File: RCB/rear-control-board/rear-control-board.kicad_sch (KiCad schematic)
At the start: 19 parts, among them J1 Conn_01x23, J2 Conn_01x14, J3 Conn_01x08, K1 T9VV1K15-12S, U3 R-78B5.0-2.0

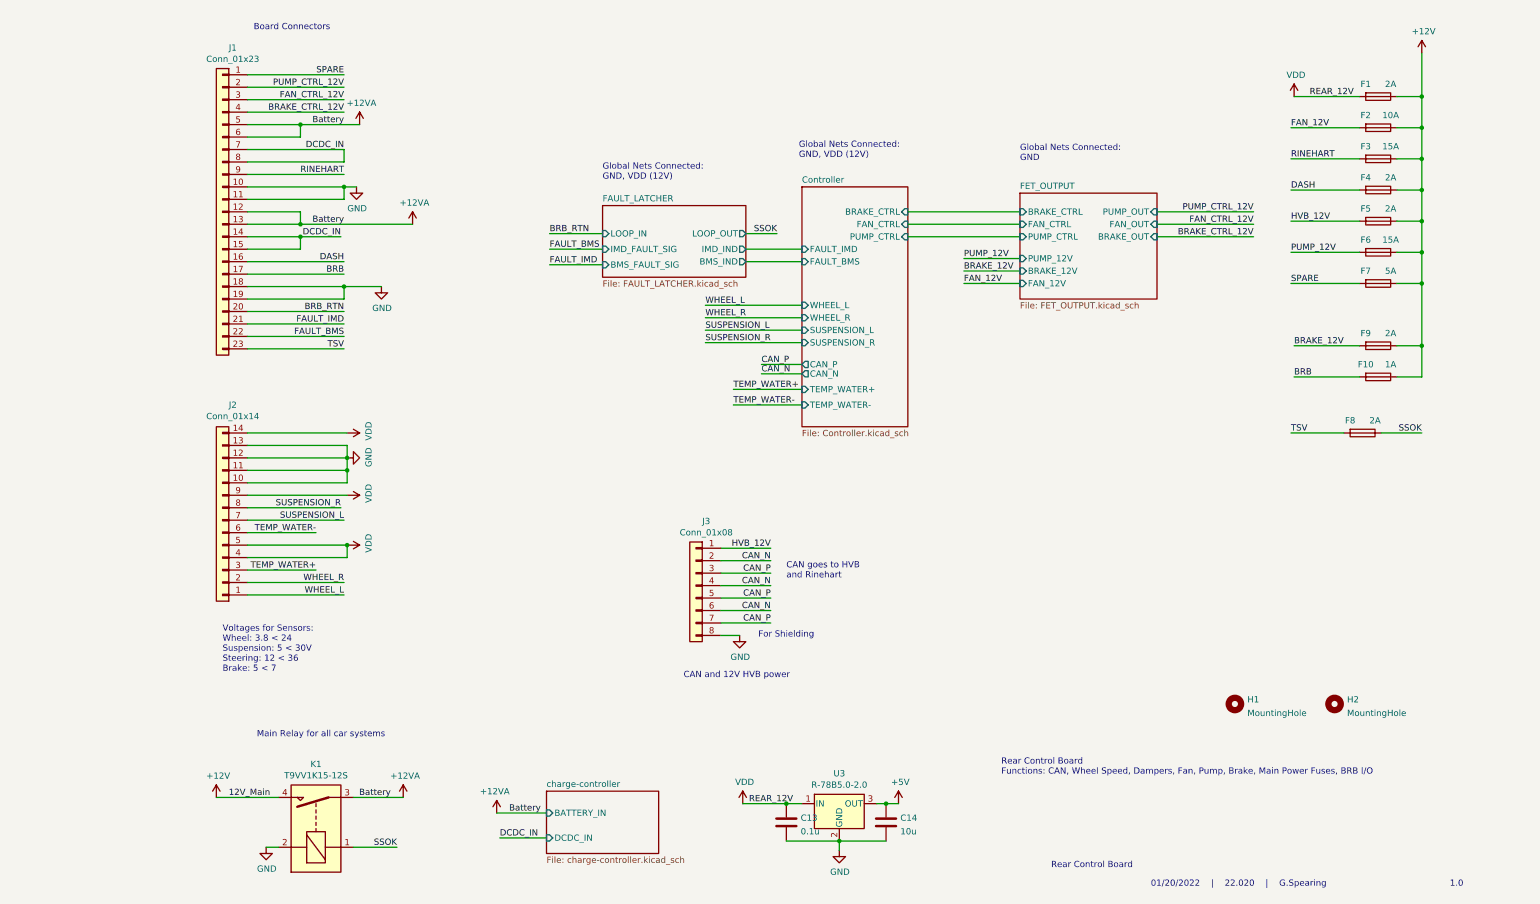
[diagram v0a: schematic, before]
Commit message: updating pinouts
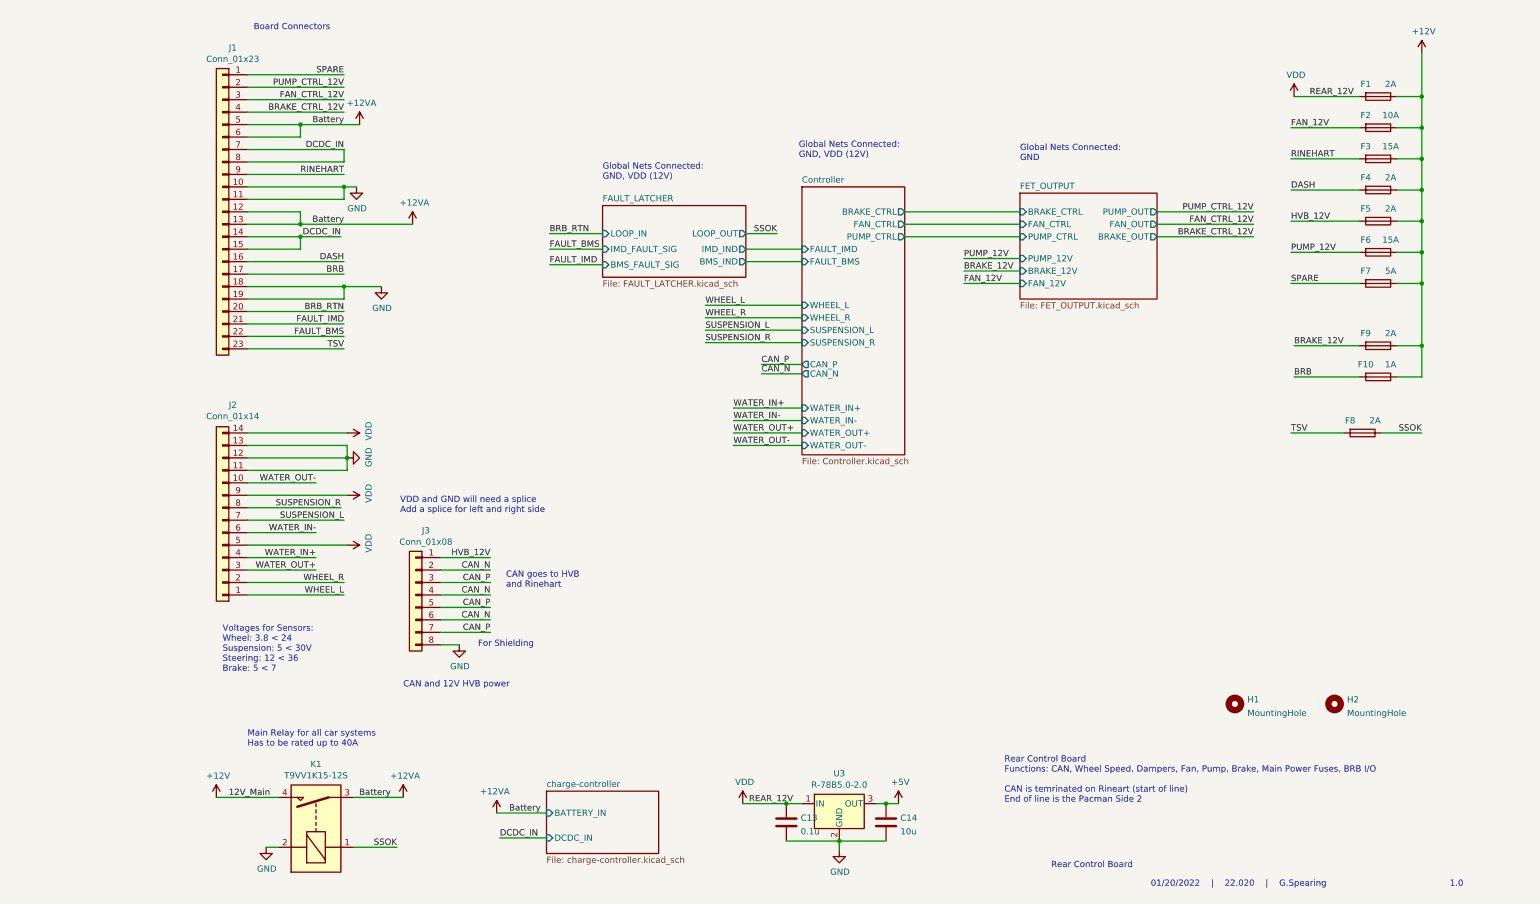
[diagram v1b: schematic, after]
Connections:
- net GND: no longer J2.10 (Pin_10)
- net VDD: no longer J2.4 (Pin_4)
- net TEMP_WATER+ renamed WATER_OUT+
- net TEMP_WATER- renamed WATER_IN-
- new net WATER_IN+: J2.4 (Pin_4)
- new net WATER_OUT-: J2.10 (Pin_10)
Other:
- sheet Controller ports: added WATER_IN+, WATER_IN-, WATER_OUT+, WATER_OUT-; removed TEMP_WATER+, TEMP_WATER-
- note added: "Main Relay for all car systems Has to be rated up to 40A"
- note added: "Rear Control Board Functions: CAN, Wheel Speed, Dampers, Fan, Pump, Brake, Main Power Fuses, BRB I/O CAN is temrinated on Rineart (start of line) End of line is the Pacman Side 2"
- note added: "VDD and GND will need a splice Add a splice for left and right side"
- note removed: "Main Relay for all car systems"
- note removed: "Rear Control Board Functions: CAN, Wheel Speed, Dampers, Fan, Pump, Brake, Main Power Fuses, BRB I/O"
- moved on the sheet: J3

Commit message: willem review notes
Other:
- note added: "DON'T FORGET INLINE FUSE FOR 12v"
- note added: "Power sensors off 5V line instead to reduce noise and help with power"
- note added: "RENAME ALL VDD TO INTERNAL 12V"
- note added: "Use VBus instead of VA"
- note added: "add sheet for fuses"
- note added: "checkout parts for temperature monitoring Look for NTC"
- note added: "protection -> TVS for the input"
- moved on the sheet: F1, F10, F2, F3, F4, F5, F6, F7, F8, F9, J1, K1

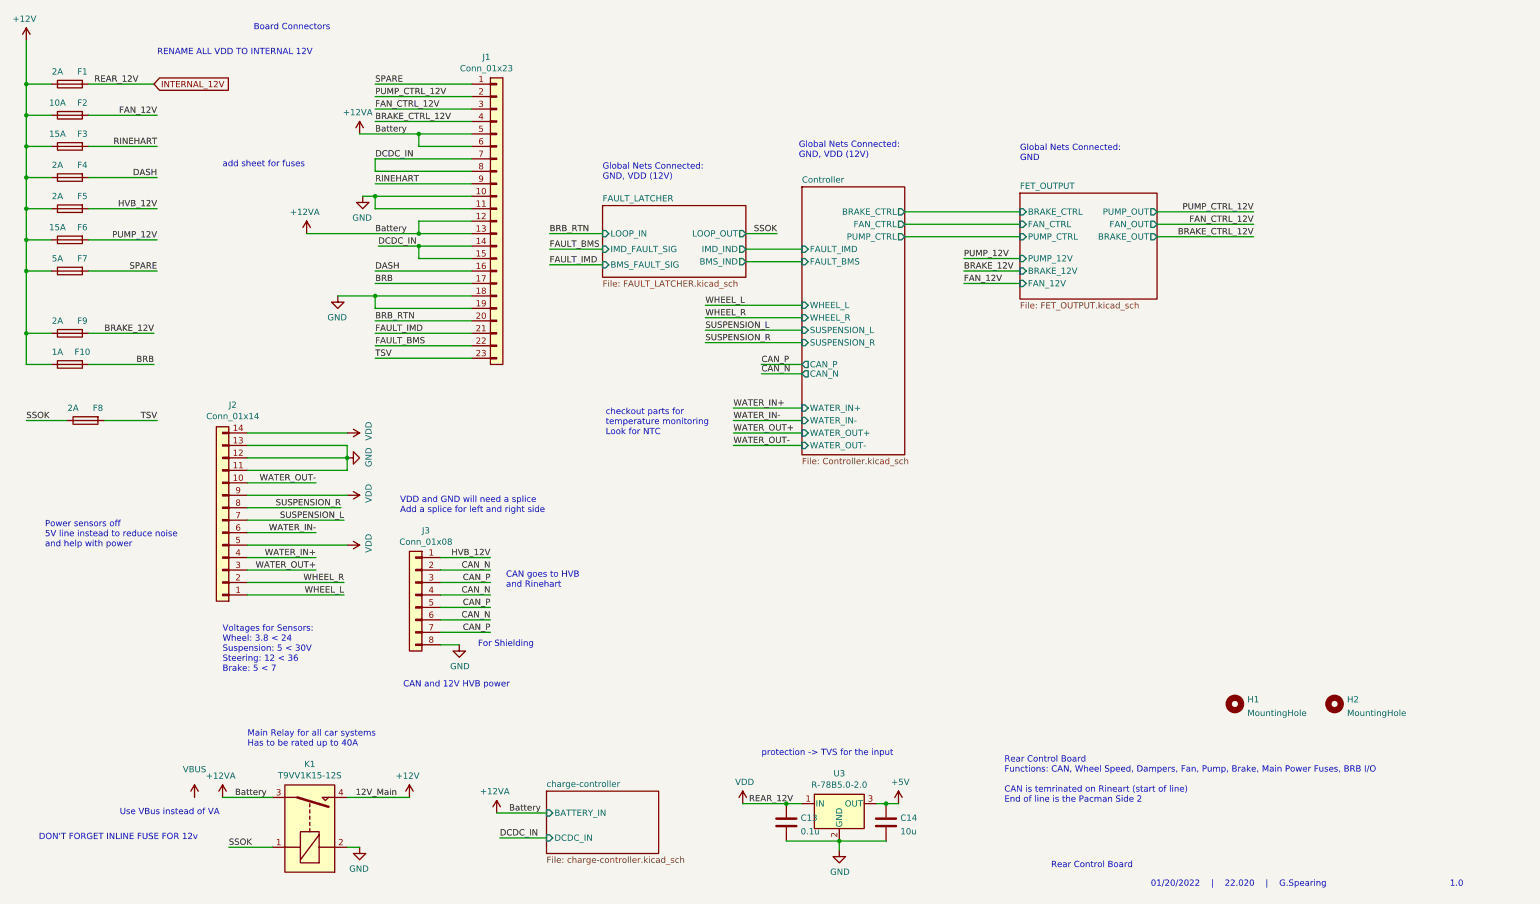
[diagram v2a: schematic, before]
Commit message: updating schem with design notes (major changes)
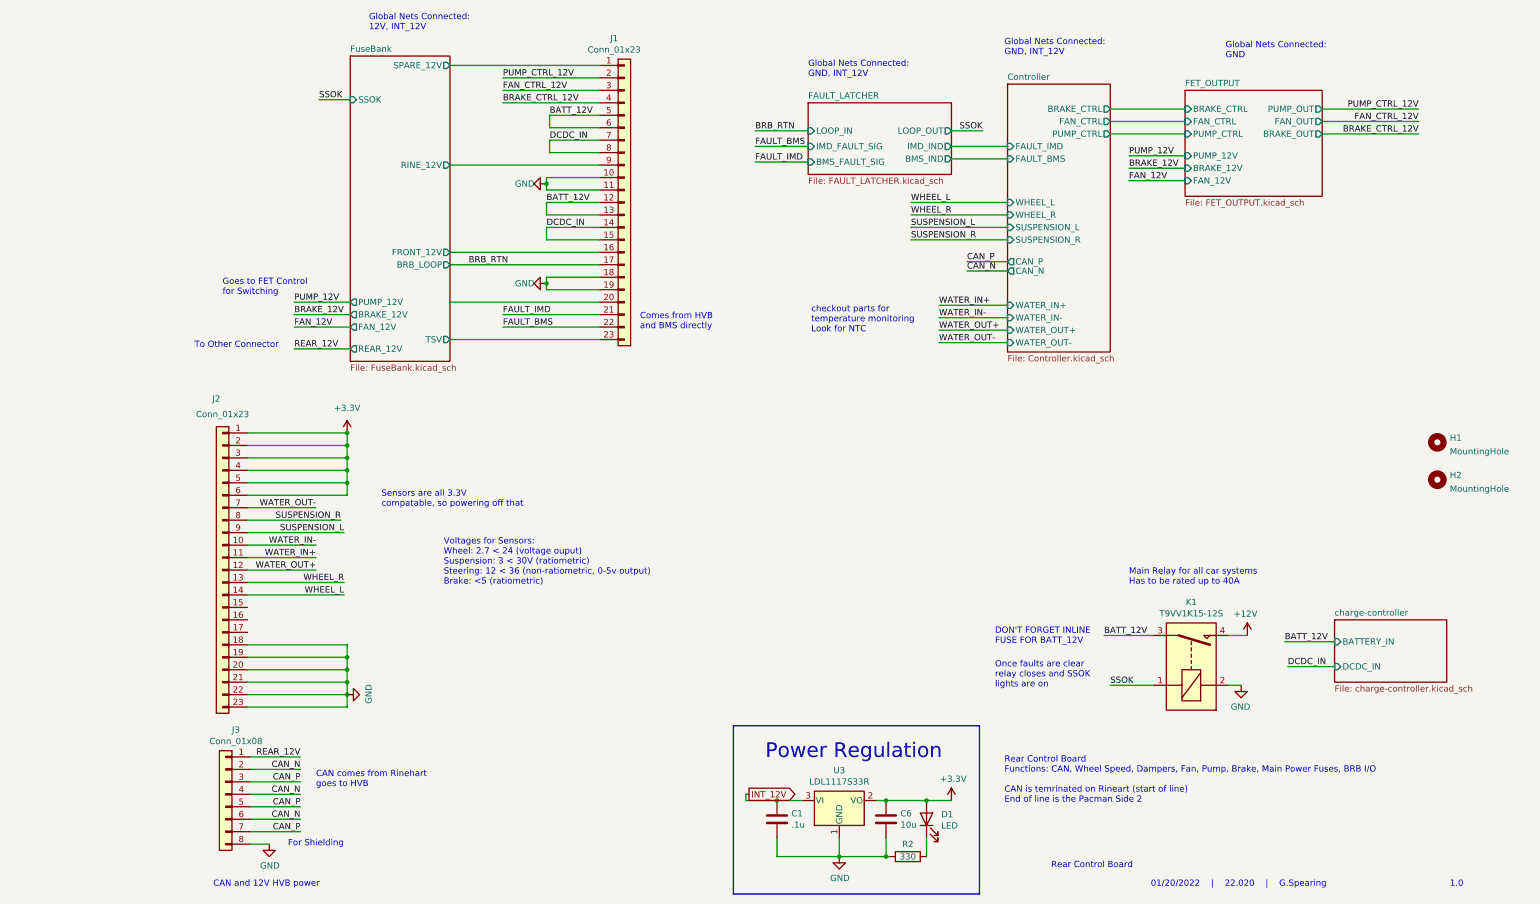
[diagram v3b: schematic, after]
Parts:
- removed C13: 0.1u, Capacitor_SMD:C_0603_1608Metric_Pad1.08x0.95mm_HandSolder, symbol Device:C
- removed C14: 10u, Capacitor_SMD:C_0603_1608Metric_Pad1.08x0.95mm_HandSolder, symbol Device:C
- removed F1, F4, F5, F8, F9: 2A, AERO_Footprints:Fuseholder_Blade_Mini_Keystone_3568, symbol Device:Fuse
- removed F10: 1A, AERO_Footprints:Fuseholder_Blade_Mini_Keystone_3568, symbol Device:Fuse
- removed F2: 10A, AERO_Footprints:Fuseholder_Blade_Mini_Keystone_3568, symbol Device:Fuse
- removed F3, F6: 15A, AERO_Footprints:Fuseholder_Blade_Mini_Keystone_3568, symbol Device:Fuse
- removed F7: 5A, AERO_Footprints:Fuseholder_Blade_Mini_Keystone_3568, symbol Device:Fuse
- removed J2: Conn_01x14, AERO_Footprints:TE_1-776266-1_14pin_Horizontal, symbol Connector_Generic:Conn_01x14
- removed U3: R-78B5.0-2.0, Converter_DCDC:Converter_DCDC_RECOM_R-78B-2.0_THT, symbol Regulator_Switching:R-78B5.0-2.0
- added C1: .1u, Capacitor_SMD:C_0603_1608Metric_Pad1.08x0.95mm_HandSolder, symbol Device:C
- added C6: 10u, Capacitor_SMD:C_0603_1608Metric_Pad1.08x0.95mm_HandSolder, symbol Device:C
- added D1: LED, LED_SMD:LED_0603_1608Metric_Pad1.05x0.95mm_HandSolder, symbol Device:LED
- added J2: Conn_01x23, AERO_Footprints:TE_1-770669-1_23pin_Horizontal, symbol Connector_Generic:Conn_01x23
- added R2: 330, Resistor_SMD:R_0603_1608Metric_Pad0.98x0.95mm_HandSolder, symbol Device:R
- added U3: LDL1117S33R, Package_TO_SOT_SMD:SOT-223-3_TabPin2, symbol Regulator_Linear:LD1117S33TR_SOT223
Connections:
- net BRB is gone; now on net BRB_RTN: J1.17 (Pin_17)
- net BRB_RTN: no longer J1.20 (Pin_20)
- net GND: now also C1.2, C6.2, J2.18 (Pin_18), J2.19 (Pin_19), J2.20 (Pin_20), J2.21 (Pin_21), J2.22 (Pin_22), J2.23 (Pin_23), R2.1, U3.1 (GND)
- net SUSPENSION_L: now also J2.9 (Pin_9)
- net SUSPENSION_R: now also J2.8 (Pin_8)
- net WATER_IN+: now also J2.11 (Pin_11)
- net WATER_IN-: now also J2.10 (Pin_10)
- net WATER_OUT+: now also J2.12 (Pin_12)
- net WATER_OUT-: now also J2.7 (Pin_7)
- net WHEEL_L: now also J2.14 (Pin_14)
- net WHEEL_R: now also J2.13 (Pin_13)
- net +12VA renamed BATT_12V
- net DASH renamed FuseBank/FRONT_12V
- net HVB_12V renamed REAR_12V
- net RINEHART renamed FuseBank/RINE_12V
- net SPARE renamed FuseBank/SPARE_12V
- net TSV renamed FuseBank/TSV
- new net: D1.1 (K), R2.2
- new net +3V3: C6.1, D1.2 (A), J2.1 (Pin_1), J2.2 (Pin_2), J2.3 (Pin_3), J2.4 (Pin_4), J2.5 (Pin_5), J2.6 (Pin_6), U3.2 (VO)
- new net INT_12V: C1.1, U3.3 (VI)
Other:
- added sheet FuseBank (FuseBank.kicad_sch)
- note added: "CAN comes from Rinehart goes to HVB"
- note added: "Comes from HVB and BMS directly"
- note added: "DON'T FORGET INLINE FUSE FOR BATT_12V"
- note added: "Global Nets Connected: 12V, INT_12V"
- note added: "Global Nets Connected: GND, INT_12V"
- note added: "Goes to FET Control for Switching"
- note added: "Once faults are clear relay closes and SSOK lights are on"
- note added: "Power Regulation"
- note added: "Sensors are all 3.3V compatable, so powering off that"
- note added: "To Other Connector"
- note added: "Voltages for Sensors: Wheel: 2.7 < 24 (voltage ouput) Suspension: 3 < 30V (ratiometric) Steering: 12 < 36 (non-ratiometric, 0-5v output) Brake: <5 (ratiometric)"
- note removed: "Board Connectors"
- note removed: "CAN goes to HVB and Rinehart"
- note removed: "DON'T FORGET INLINE FUSE FOR 12v"
- note removed: "Global Nets Connected: GND, VDD (12V)"
- note removed: "Power sensors off 5V line instead to reduce noise and help with power"
- note removed: "RENAME ALL VDD TO INTERNAL 12V"
- note removed: "Use VBus instead of VA"
- note removed: "VDD and GND will need a splice Add a splice for left and right side"
- note removed: "Voltages for Sensors: Wheel: 3.8 < 24 Suspension: 5 < 30V Steering: 12 < 36 Brake: 5 < 7"
- note removed: "add sheet for fuses"
- note removed: "protection -> TVS for the input"
- moved on the sheet: H1, H2, J1, J3, K1

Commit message: minor layout changes based on schem updates
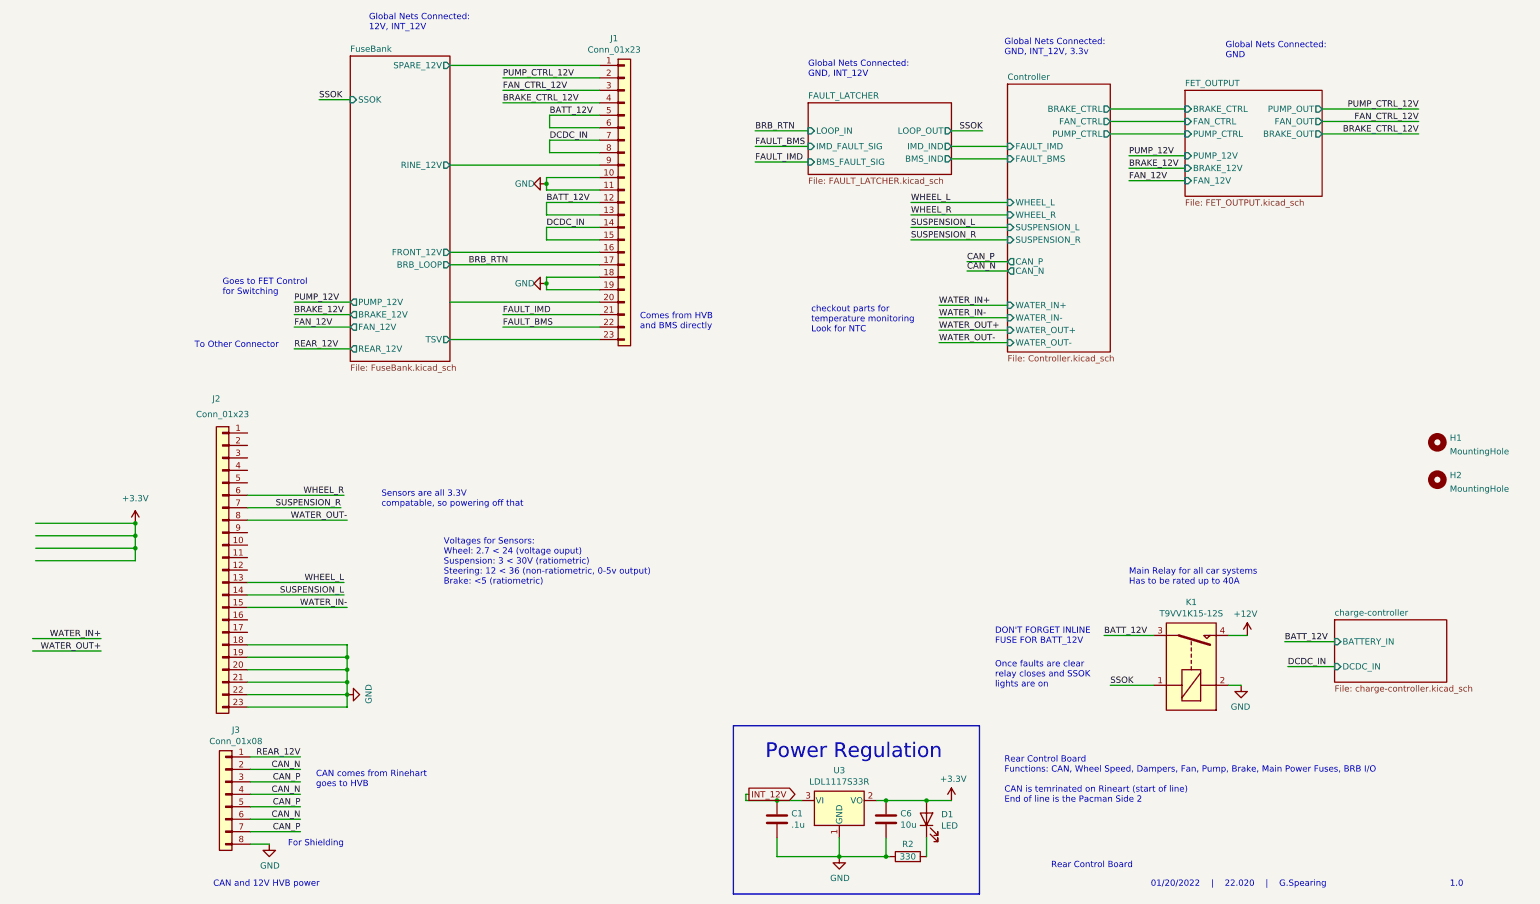
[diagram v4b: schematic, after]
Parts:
- K1: footprint AERO_Footprints:RELAY_T9VV1K15-12S -> AERO-footprints:RELAY_T9VV1K15-12S
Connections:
- net +3V3: no longer J2.1 (Pin_1), J2.2 (Pin_2), J2.3 (Pin_3), J2.4 (Pin_4), J2.5 (Pin_5), J2.6 (Pin_6)
- net SUSPENSION_L: now also J2.14 (Pin_14); no longer J2.9 (Pin_9)
- net SUSPENSION_R: now also J2.7 (Pin_7); no longer J2.8 (Pin_8)
- net WATER_IN+: no longer J2.11 (Pin_11)
- net WATER_IN-: now also J2.15 (Pin_15); no longer J2.10 (Pin_10)
- net WATER_OUT+: no longer J2.12 (Pin_12)
- net WATER_OUT-: now also J2.8 (Pin_8); no longer J2.7 (Pin_7)
- net WHEEL_L: now also J2.13 (Pin_13); no longer J2.14 (Pin_14)
- net WHEEL_R: now also J2.6 (Pin_6); no longer J2.13 (Pin_13)
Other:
- note added: "Global Nets Connected: GND, INT_12V, 3.3v"
